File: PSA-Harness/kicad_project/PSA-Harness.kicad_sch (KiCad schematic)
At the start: 11 parts, among them J1 to_car_3, J2 to_ESP_3, J3 to_car_2, J4 to_EPS_2, J5 to_car_1, J6 to_EPS_1, J7 USB_C_Receptacle, K1 G6K-2G-Y DC5

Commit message: chg: add doc images, upgrade to kicad 9
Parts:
- renumbered J6 to J1, J4 to J2, J2 to J3, J5 to J4, J3 to J5, J1 to J6
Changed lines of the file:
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@@
 (kicad_sch
-	(version 20231120)
+	(version 20250114)
 	(generator "eeschema")
-	(generator_version "8.0")
+	(generator_version "9.0")
 	(paper "A4")
+	(text "Harness Connector"
+		(exclude_from_sim no)
+		(at 68.072 30.734 0)
+		(effects
+			(font
+				(size 2 2)
+			)
+			(justify left bottom)
+		)
+	)
+	(text "OBD-C Connector"
+		(exclude_from_sim no)
+		(at 229.87 30.48 0)
+		(effects
+			(font
+				(size 2 2)
+			)
+			(justify left bottom)
+		)
+	)
+	(text "Relay"
+		(exclude_from_sim no)
+		(at 165.1 30.48 0)
+		(effects
+			(font
+				(size 2 2)
+			)
+			(justify left bottom)
+		)
+	)
 	(junction
 		(at 165.1 55.88)
@@
 		)
 	)
-	(text "Harness Connector"
-		(exclude_from_sim no)
-		(at 68.072 30.734 0)
-		(effects
-			(font
-				(size 2 2)
-			)
-			(justify left bottom)
-		)
-	)
-	(text "OBD-C Connector"
-		(exclude_from_sim no)
-		(at 229.87 30.48 0)
-		(effects
-			(font
-				(size 2 2)
-			)
-			(justify left bottom)
-		)
-	)
-	(text "Relay"
-		(exclude_from_sim no)
-		(at 165.1 30.48 0)
-		(effects
-			(font
-				(size 2 2)
-			)
-			(justify left bottom)
-		)
-	)
 	(global_label "51"
 		(shape input)
@@
 		(on_board yes)
 		(dnp no)
-		(property "Reference" "J1"
+		(property "Reference" "J6"
 			(at 118.11 76.2 0)
 			(effects
@@
 		(on_board yes)
 		(dnp no)
-		(property "Reference" "J4"
+		(property "Reference" "J2"
 			(at 87.63 34.29 0)
 			(effects
@@
 		(on_board yes)
 		(dnp no)
-		(property "Reference" "J3"
+		(property "Reference" "J5"
 			(at 87.63 76.2 0)
 			(effects
@@
 		(on_board yes)
 		(dnp no)
-		(property "Reference" "J5"
+		(property "Reference" "J4"
 			(at 57.15 76.2 0)
 			(effects
@@
 		(on_board yes)
 		(dnp no)
-		(property "Reference" "J6"
+		(property "Reference" "J1"
 			(at 57.15 34.29 0)
 			(effects
@@
 		(on_board yes)
 		(dnp no)
-		(property "Reference" "J2"
+		(property "Reference" "J3"
 			(at 118.11 34.29 0)
 			(effects
@@
 		)
 	)
+	(embedded_fonts no)
 )

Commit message: chg: use correct footprints, SMD socket clearence too low
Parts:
- J1, J2, J3: footprint PSA:PinSocket_2x10_P2.54mm_Vertical_SMD_PSA -> PSA:TSM-110-03-X-DV
- J4, J5, J6: footprint PSA:PinHeader_2x10_P2.54mm_Vertical_SMD_PSA_small -> PSA:SSW-110-22-F-D-VS-K-TR
- J7: footprint PSA:TYPE-C-31-M-04 -> PSA:GCT_USB4115-03-C_REVB4
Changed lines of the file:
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@@
 			)
 		)
-		(property "Footprint" "PSA:PinHeader_2x10_P2.54mm_Vertical_SMD_PSA_small"
+		(property "Footprint" "PSA:SSW-110-22-F-D-VS-K-TR"
 			(at 116.84 92.71 0)
 			(effects
@@
 			)
 		)
-		(property "Footprint" "PSA:PinSocket_2x10_P2.54mm_Vertical_SMD_PSA"
+		(property "Footprint" "PSA:TSM-110-03-X-DV"
 			(at 86.36 50.8 0)
 			(effects
@@
 			)
 		)
-		(property "Footprint" "PSA:TYPE-C-31-M-04"
+		(property "Footprint" "PSA:GCT_USB4115-03-C_REVB4"
 			(at 246.38 82.55 0)
 			(effects
@@
 			)
 		)
-		(property "Footprint" "PSA:PinHeader_2x10_P2.54mm_Vertical_SMD_PSA_small"
+		(property "Footprint" "PSA:SSW-110-22-F-D-VS-K-TR"
 			(at 86.36 92.71 0)
 			(effects
@@
 			)
 		)
-		(property "Footprint" "PSA:PinHeader_2x10_P2.54mm_Vertical_SMD_PSA_small"
+		(property "Footprint" "PSA:SSW-110-22-F-D-VS-K-TR"
 			(at 55.88 92.71 0)
 			(effects
@@
 			)
 		)
-		(property "Footprint" "PSA:PinSocket_2x10_P2.54mm_Vertical_SMD_PSA"
+		(property "Footprint" "PSA:TSM-110-03-X-DV"
 			(at 55.88 50.8 0)
 			(effects
@@
 			)
 		)
-		(property "Footprint" "PSA:PinSocket_2x10_P2.54mm_Vertical_SMD_PSA"
+		(property "Footprint" "PSA:TSM-110-03-X-DV"
 			(at 116.84 50.8 0)
 			(effects

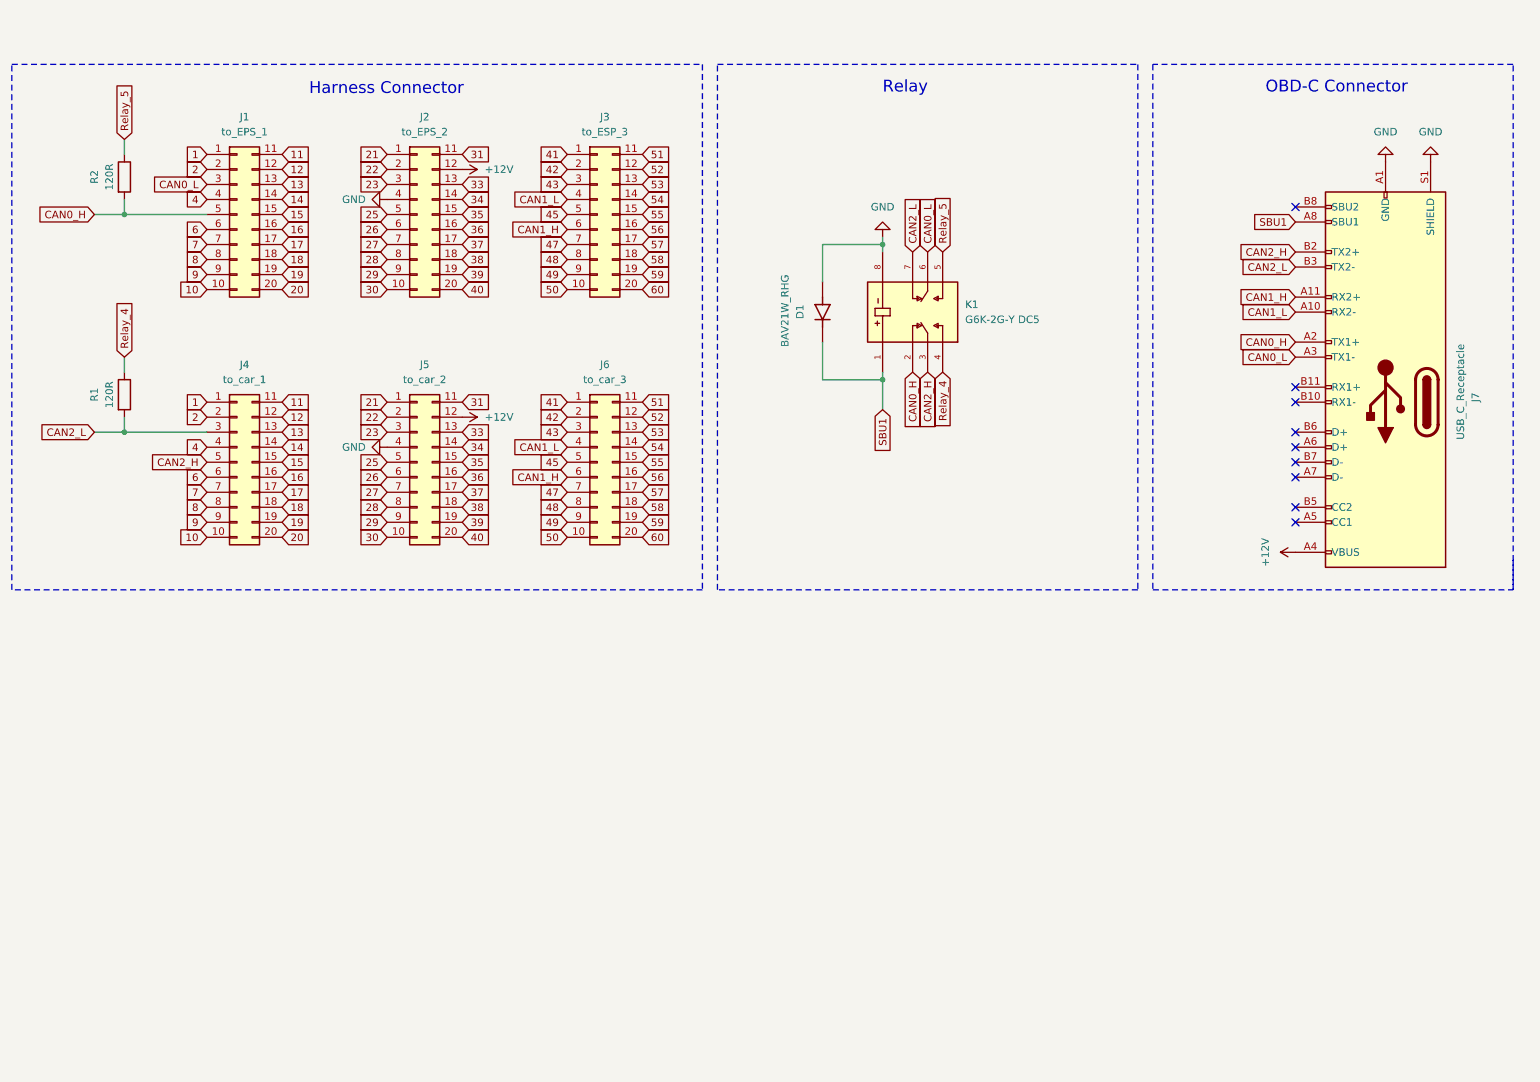
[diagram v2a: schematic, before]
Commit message: chg: stacked PCBs
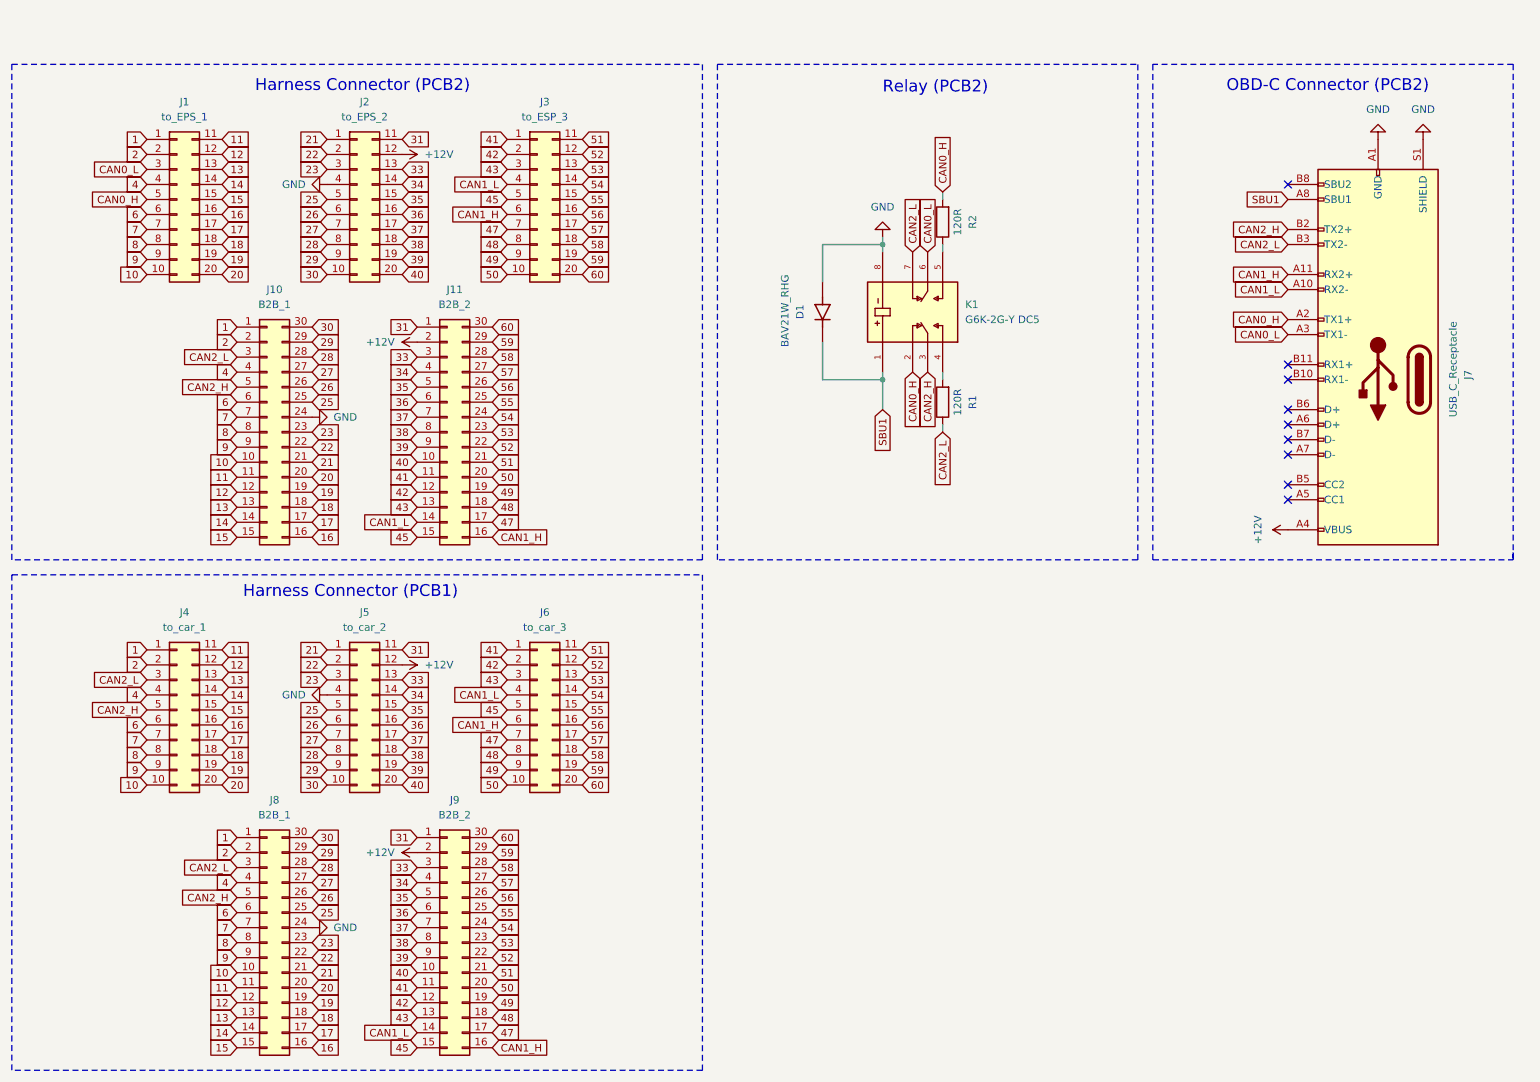
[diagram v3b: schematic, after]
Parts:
- added J10, J8: B2B_1, Connector_PinHeader_1.27mm:PinHeader_2x15_P1.27mm_Vertical, symbol Connector_Generic:Conn_02x15_Counter_Clockwise
- added J11, J9: B2B_2, Connector_PinHeader_1.27mm:PinHeader_2x15_P1.27mm_Vertical, symbol Connector_Generic:Conn_02x15_Counter_Clockwise
- J1, J2, J3: footprint PSA:TSM-110-03-X-DV -> Connector_PinHeader_2.54mm:PinHeader_2x10_P2.54mm_Vertical
- J4, J5, J6: footprint PSA:SSW-110-22-F-D-VS-K-TR -> Connector_PinSocket_2.54mm:PinSocket_2x10_P2.54mm_Vertical
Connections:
- net +12V: now also J11.2 (Pin_2), J9.2 (Pin_2)
- net 1: now also J10.1 (Pin_1), J8.1 (Pin_1)
- net 10: now also J10.10 (Pin_10), J8.10 (Pin_10)
- net 11: now also J10.11 (Pin_11), J8.11 (Pin_11)
- net 12: now also J10.12 (Pin_12), J8.12 (Pin_12)
- net 13: now also J10.13 (Pin_13), J8.13 (Pin_13)
- net 14: now also J10.14 (Pin_14), J8.14 (Pin_14)
- net 15: now also J10.15 (Pin_15), J8.15 (Pin_15)
- net 16: now also J10.16 (Pin_16), J8.16 (Pin_16)
- net 17: now also J10.17 (Pin_17), J8.17 (Pin_17)
- net 18: now also J10.18 (Pin_18), J8.18 (Pin_18)
- net 19: now also J10.19 (Pin_19), J8.19 (Pin_19)
- net 2: now also J10.2 (Pin_2), J8.2 (Pin_2)
- net 20: now also J10.20 (Pin_20), J8.20 (Pin_20)
- net 21: now also J10.21 (Pin_21), J8.21 (Pin_21)
- net 22: now also J10.22 (Pin_22), J8.22 (Pin_22)
- net 23: now also J10.23 (Pin_23), J8.23 (Pin_23)
- net 25: now also J10.25 (Pin_25), J8.25 (Pin_25)
- net 26: now also J10.26 (Pin_26), J8.26 (Pin_26)
- net 27: now also J10.27 (Pin_27), J8.27 (Pin_27)
- net 28: now also J10.28 (Pin_28), J8.28 (Pin_28)
- net 29: now also J10.29 (Pin_29), J8.29 (Pin_29)
- net 30: now also J10.30 (Pin_30), J8.30 (Pin_30)
- net 31: now also J11.1 (Pin_1), J9.1 (Pin_1)
- net 33: now also J11.3 (Pin_3), J9.3 (Pin_3)
- net 34: now also J11.4 (Pin_4), J9.4 (Pin_4)
- net 35: now also J11.5 (Pin_5), J9.5 (Pin_5)
- net 36: now also J11.6 (Pin_6), J9.6 (Pin_6)
- net 37: now also J11.7 (Pin_7), J9.7 (Pin_7)
- net 38: now also J11.8 (Pin_8), J9.8 (Pin_8)
- net 39: now also J11.9 (Pin_9), J9.9 (Pin_9)
- net 4: now also J10.4 (Pin_4), J8.4 (Pin_4)
- net 40: now also J11.10 (Pin_10), J9.10 (Pin_10)
- net 41: now also J11.11 (Pin_11), J9.11 (Pin_11)
- net 42: now also J11.12 (Pin_12), J9.12 (Pin_12)
- net 43: now also J11.13 (Pin_13), J9.13 (Pin_13)
- net 45: now also J11.15 (Pin_15), J9.15 (Pin_15)
- net 47: now also J11.17 (Pin_17), J9.17 (Pin_17)
- net 48: now also J11.18 (Pin_18), J9.18 (Pin_18)
- net 49: now also J11.19 (Pin_19), J9.19 (Pin_19)
- net 50: now also J11.20 (Pin_20), J9.20 (Pin_20)
- net 51: now also J11.21 (Pin_21), J9.21 (Pin_21)
- net 52: now also J11.22 (Pin_22), J9.22 (Pin_22)
- net 53: now also J11.23 (Pin_23), J9.23 (Pin_23)
- net 54: now also J11.24 (Pin_24), J9.24 (Pin_24)
- net 55: now also J11.25 (Pin_25), J9.25 (Pin_25)
- net 56: now also J11.26 (Pin_26), J9.26 (Pin_26)
- net 57: now also J11.27 (Pin_27), J9.27 (Pin_27)
- net 58: now also J11.28 (Pin_28), J9.28 (Pin_28)
- net 59: now also J11.29 (Pin_29), J9.29 (Pin_29)
- net 6: now also J10.6 (Pin_6), J8.6 (Pin_6)
- net 60: now also J11.30 (Pin_30), J9.30 (Pin_30)
- net 7: now also J10.7 (Pin_7), J8.7 (Pin_7)
- net 8: now also J10.8 (Pin_8), J8.8 (Pin_8)
- net 9: now also J10.9 (Pin_9), J8.9 (Pin_9)
- net CAN1_H: now also J11.16 (Pin_16), J9.16 (Pin_16)
- net CAN1_L: now also J11.14 (Pin_14), J9.14 (Pin_14)
- net CAN2_H: now also J10.5 (Pin_5), J8.5 (Pin_5)
- net CAN2_L: now also R1.1, J10.3 (Pin_3), J8.3 (Pin_3); no longer R1.2
- net GND: now also J10.24 (Pin_24), J8.24 (Pin_24)
- net Relay_4: no longer names the net of K1.4
- net Relay_4: now also R1.2; no longer R1.1
- net Relay_5: no longer names the net of K1.5, R2.1
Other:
- note added: "Harness Connector (PCB1)"
- note added: "Harness Connector (PCB2)"
- note added: "OBD-C Connector (PCB2)"
- note added: "Relay (PCB2)"
- note removed: "Harness Connector"
- note removed: "OBD-C Connector"
- note removed: "Relay"
- moved on the sheet: J1, J2, J3, J4, J5, J6, J7, R1, R2

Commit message: reduce clearances
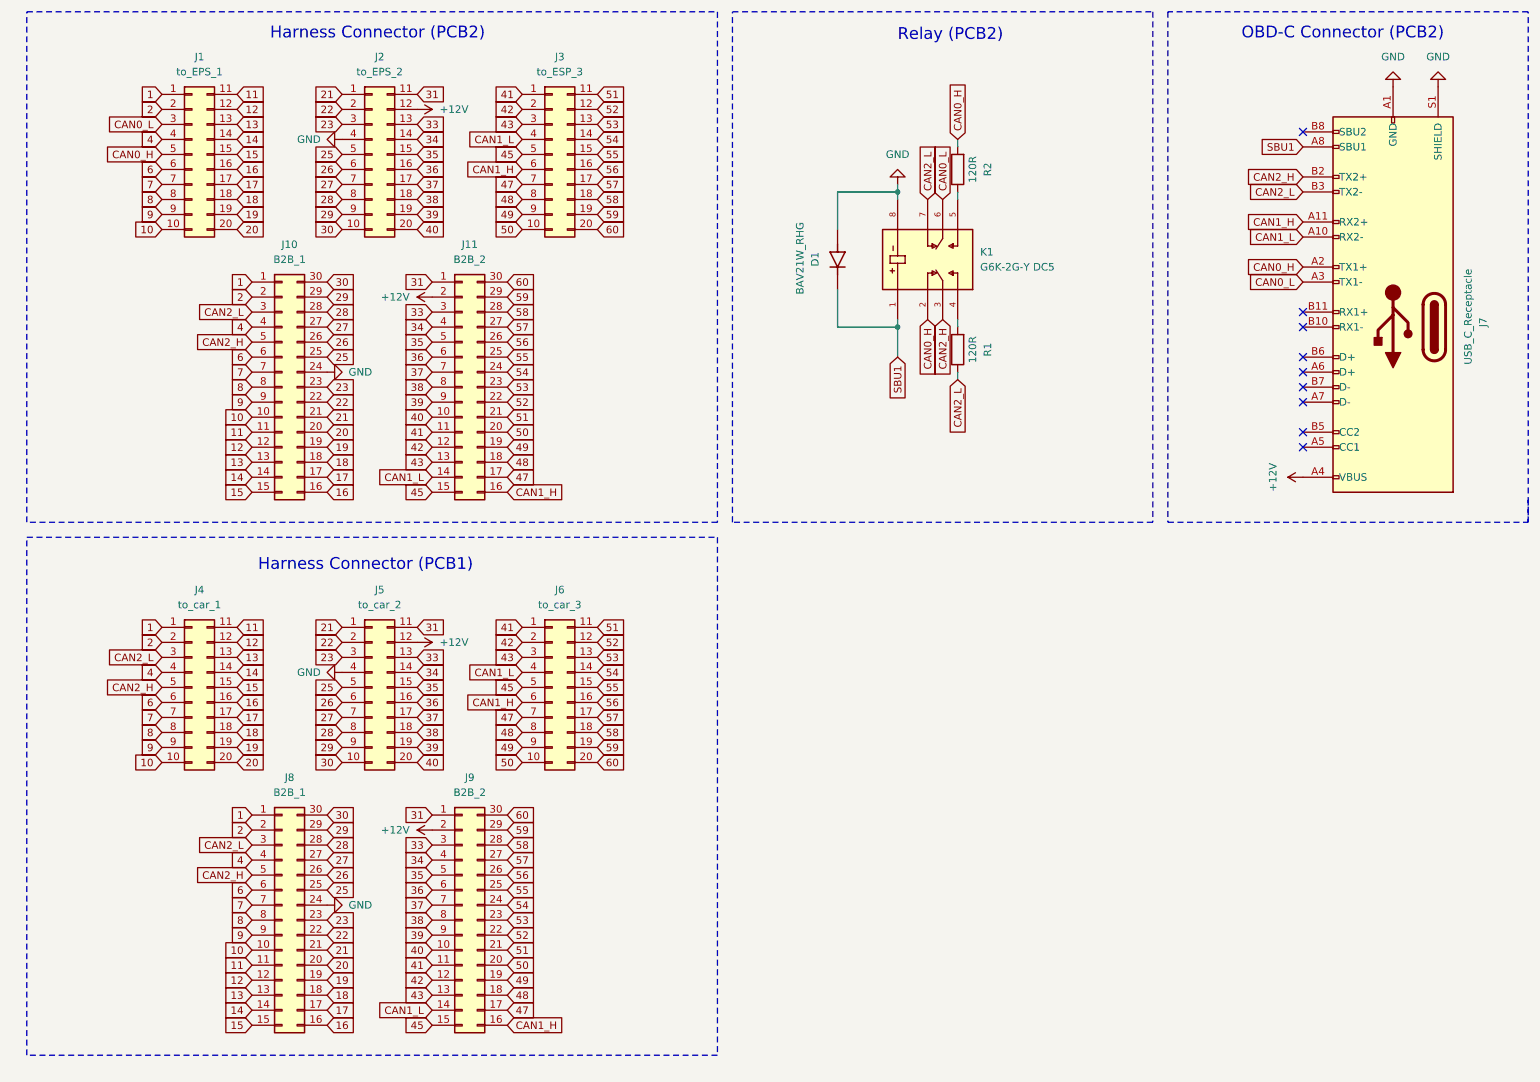
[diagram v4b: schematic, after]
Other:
- moved on the sheet: D1, J1, J10, J11, J2, J3, J4, J5, J6, J7, J8, J9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

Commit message: add: connector footprints
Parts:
- J1, J2, J3: footprint Connector_PinHeader_2.54mm:PinHeader_2x10_P2.54mm_Vertical -> PSA:10129381-920003BLF
- J4, J5, J6: footprint Connector_PinSocket_2.54mm:PinSocket_2x10_P2.54mm_Vertical -> PSA:ESW-110-44-F-D
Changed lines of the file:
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@@
 			)
 		)
-		(property "Footprint" "Connector_PinSocket_2.54mm:PinSocket_2x10_P2.54mm_Vertical"
+		(property "Footprint" "PSA:ESW-110-44-F-D"
 			(at 109.22 130.81 0)
 			(effects
@@
 			)
 		)
-		(property "Footprint" "Connector_PinHeader_2.54mm:PinHeader_2x10_P2.54mm_Vertical"
+		(property "Footprint" "PSA:10129381-920003BLF"
 			(at 78.74 40.64 0)
 			(effects
@@
 			)
 		)
-		(property "Footprint" "Connector_PinSocket_2.54mm:PinSocket_2x10_P2.54mm_Vertical"
+		(property "Footprint" "PSA:ESW-110-44-F-D"
 			(at 78.74 130.81 0)
 			(effects
@@
 			)
 		)
-		(property "Footprint" "Connector_PinSocket_2.54mm:PinSocket_2x10_P2.54mm_Vertical"
+		(property "Footprint" "PSA:ESW-110-44-F-D"
 			(at 48.26 130.81 0)
 			(effects
@@
 			)
 		)
-		(property "Footprint" "Connector_PinHeader_2.54mm:PinHeader_2x10_P2.54mm_Vertical"
+		(property "Footprint" "PSA:10129381-920003BLF"
 			(at 48.26 40.64 0)
 			(effects
@@
 			)
 		)
-		(property "Footprint" "Connector_PinHeader_2.54mm:PinHeader_2x10_P2.54mm_Vertical"
+		(property "Footprint" "PSA:10129381-920003BLF"
 			(at 109.22 40.64 0)
 			(effects
